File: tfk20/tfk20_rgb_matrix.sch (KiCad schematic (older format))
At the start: 40 parts

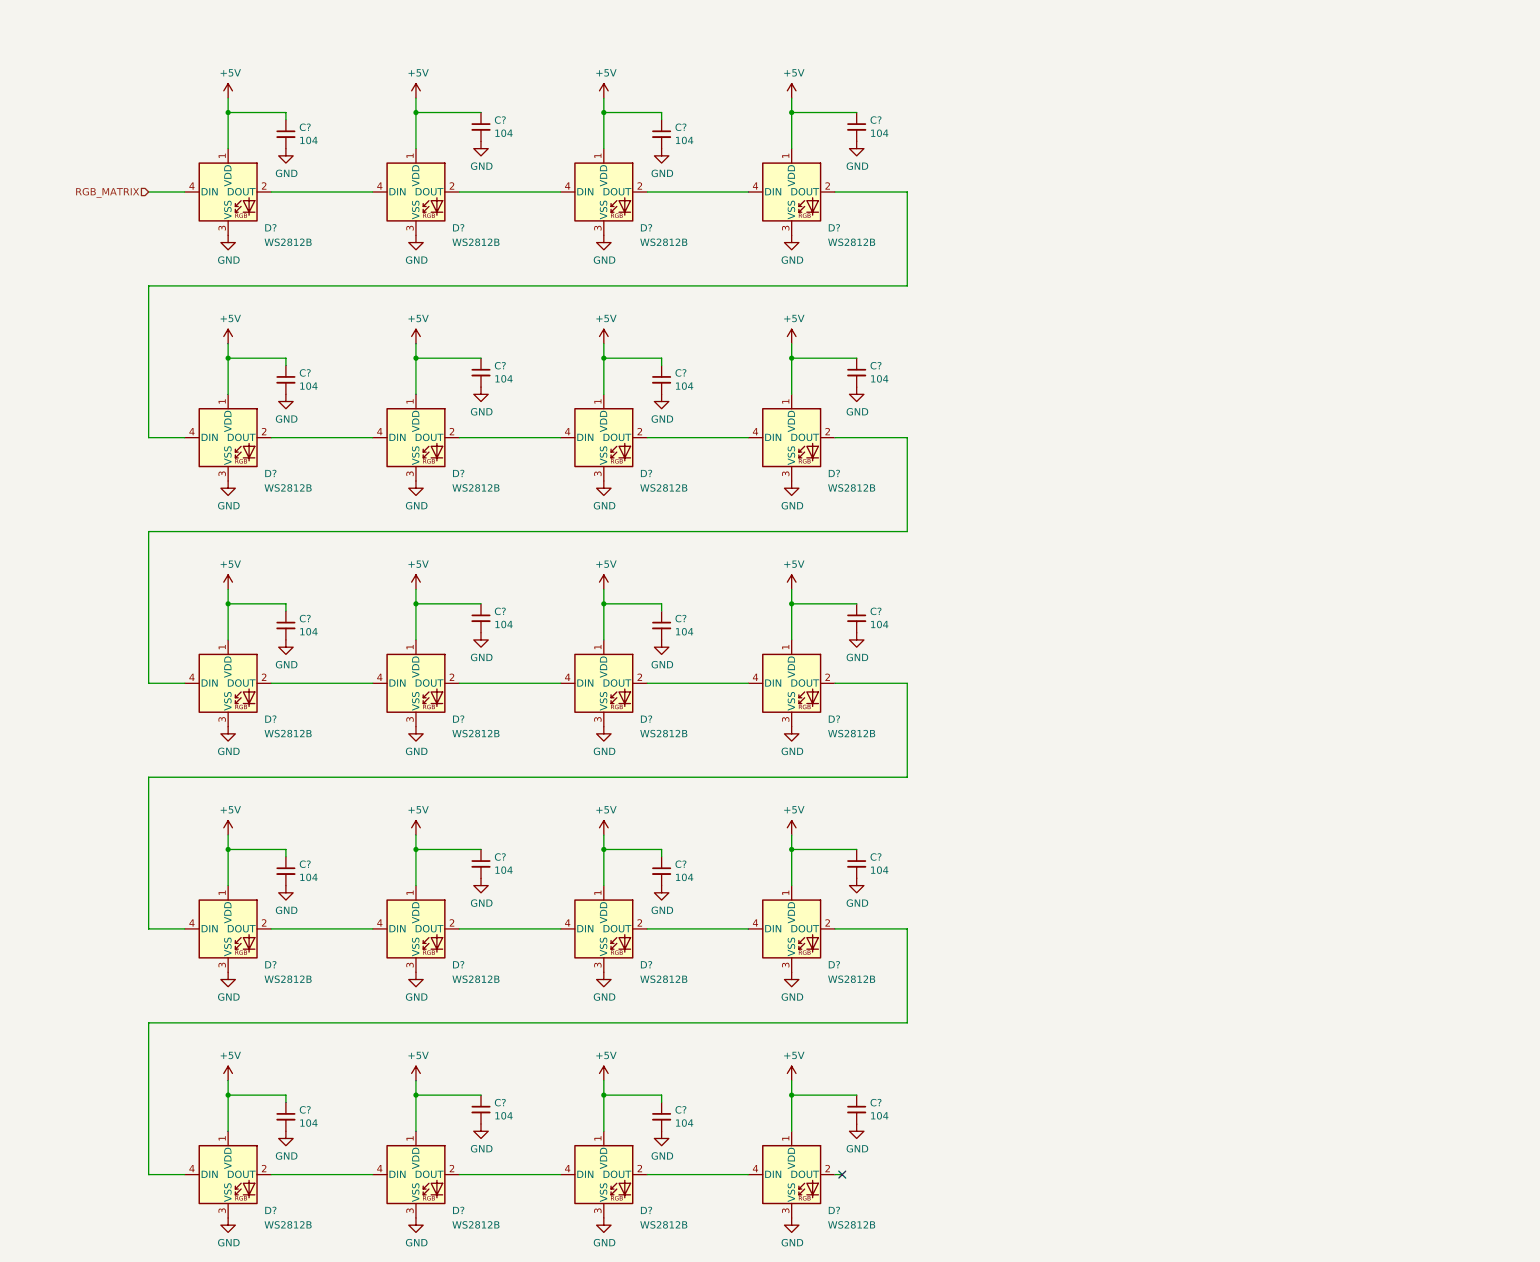
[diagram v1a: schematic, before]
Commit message: RGB LED driver
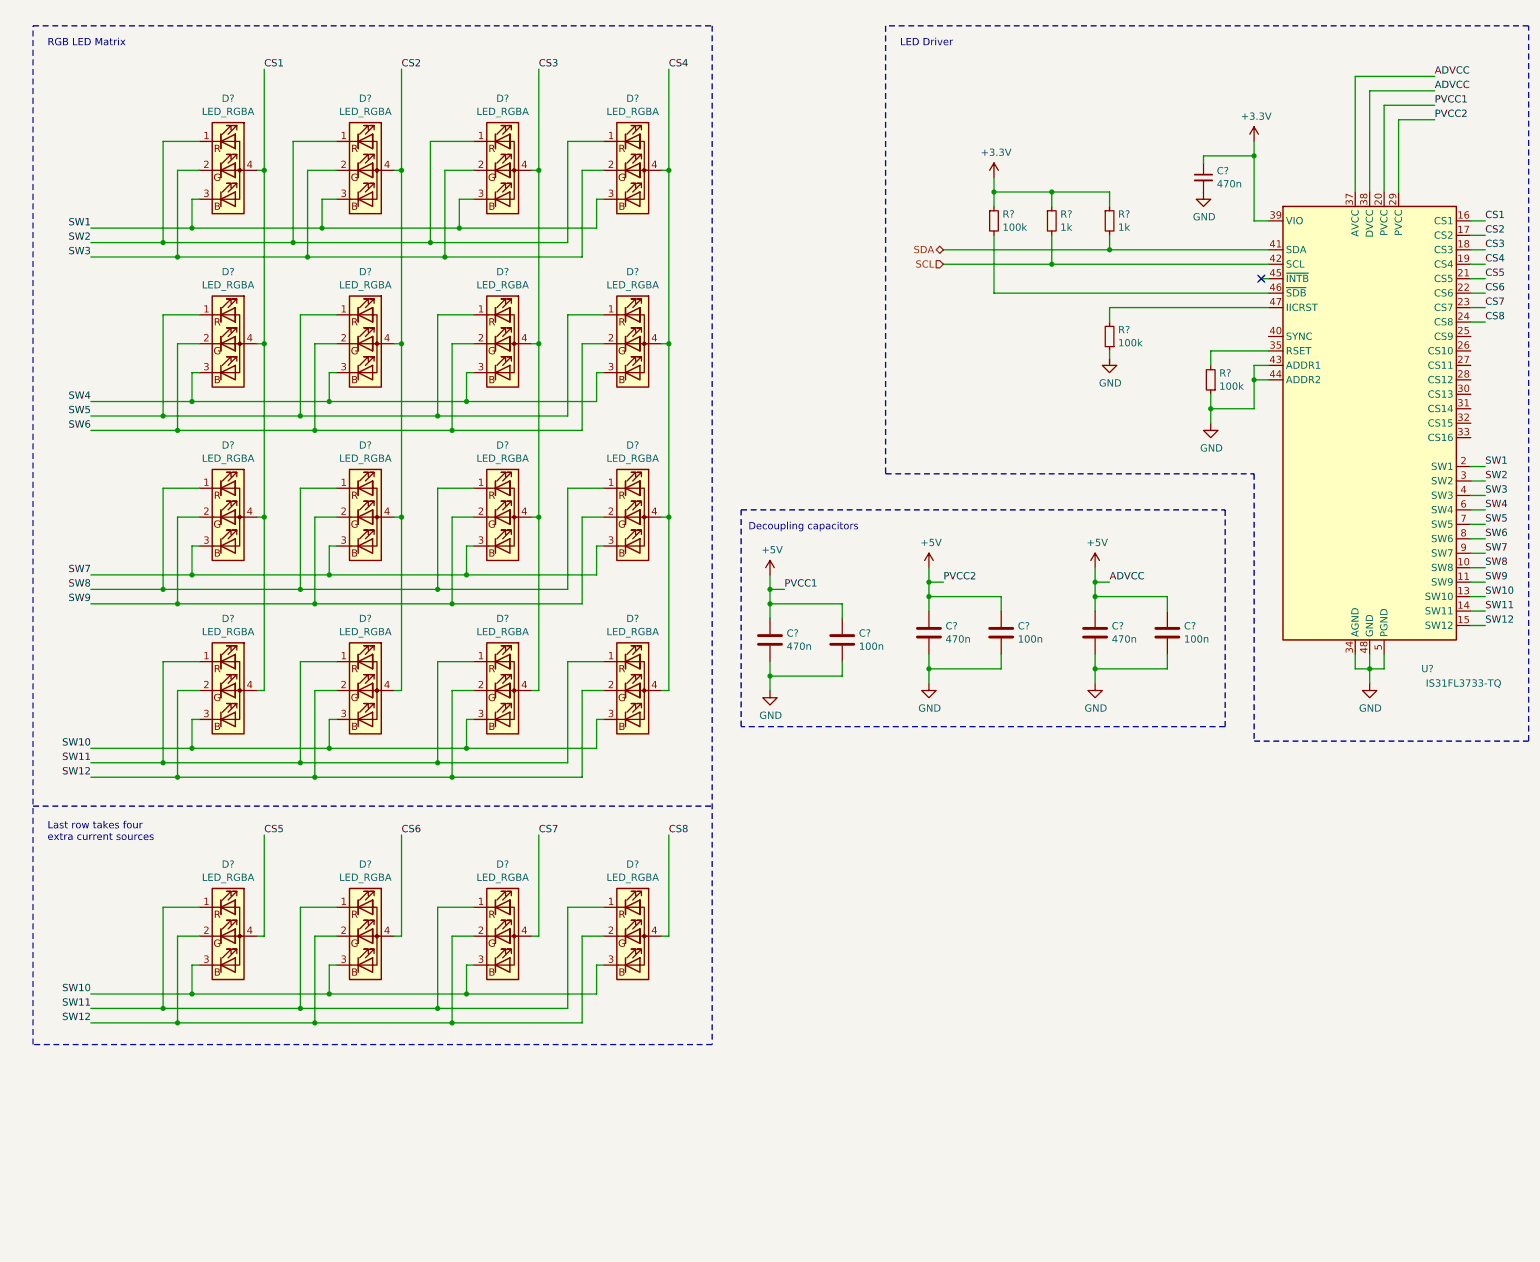
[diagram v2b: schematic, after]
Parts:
- removed C? (x20): 104, symbol Device:C_Small
- removed D? (x20): WS2812B, LED_SMD:LED_WS2812B_PLCC4_5.0x5.0mm_P3.2mm, symbol LED:WS2812B
- added C?: 470n, symbol Device:C_Small
- added C? (x3): 470n, symbol Device:C
- added C? (x3): 100n, symbol Device:C
- added D? (x20): LED_RGBA, symbol Device:LED_RGBA
- added R? (x3): 100k, symbol Device:R_Small
- added R? (x2): 1k, symbol Device:R_Small
- added U?: IS31FL3733-TQ, Package_QFP:TQFP-48-1EP_7x7mm_P0.5mm_EP5x5mm, symbol Driver_LED:IS31FL3733-TQ
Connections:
- net +5V: now also C?.1, C?.1, C?.1, C?.1, C?.1, C?.2, U?.20 (PVCC), U?.29 (PVCC), U?.37 (AVCC), U?.38 (DVCC)
- net GND: now also C?.1, C?.2, C?.2, C?.2, C?.2, C?.2, C?.2, R?.1, R?.1, U?.12 (PGND), U?.34 (AGND), U?.43 (ADDR1), U?.44 (ADDR2), U?.48 (GND), U?.49 (GND), U?.5 (PGND)
- new net: R?.2, U?.35 (RSET)
- new net: R?.2, U?.46 (~SDB)
- new net: R?.2, U?.47 (IICRST)
- new net +3V3: C?.1, R?.1, R?.1, R?.1, U?.39 (VIO)
- new net CS1: D?.4 (A), D?.4 (A), D?.4 (A), D?.4 (A), U?.16 (CS1)
- new net CS2: D?.4 (A), D?.4 (A), D?.4 (A), D?.4 (A), U?.17 (CS2)
- new net CS3: D?.4 (A), D?.4 (A), D?.4 (A), D?.4 (A), U?.18 (CS3)
- new net CS4: D?.4 (A), D?.4 (A), D?.4 (A), D?.4 (A), U?.19 (CS4)
- new net CS5: D?.4 (A), U?.21 (CS5)
- new net CS6: D?.4 (A), U?.22 (CS6)
- new net CS7: D?.4 (A), U?.23 (CS7)
- new net CS8: D?.4 (A), U?.24 (CS8)
- new net SCL: R?.2, U?.42 (SCL)
- new net SDA: R?.2, U?.41 (SDA)
- new net SW1: D?.3 (BK), D?.3 (BK), D?.3 (BK), D?.3 (BK), U?.2 (SW1)
- new net SW10: D?.3 (BK), D?.3 (BK), D?.3 (BK), D?.3 (BK), D?.3 (BK), D?.3 (BK), D?.3 (BK), D?.3 (BK), U?.13 (SW10)
- new net SW11: D?.1 (RK), D?.1 (RK), D?.1 (RK), D?.1 (RK), D?.1 (RK), D?.1 (RK), D?.1 (RK), D?.1 (RK), U?.14 (SW11)
- new net SW12: D?.2 (GK), D?.2 (GK), D?.2 (GK), D?.2 (GK), D?.2 (GK), D?.2 (GK), D?.2 (GK), D?.2 (GK), U?.15 (SW12)
- new net SW2: D?.1 (RK), D?.1 (RK), D?.1 (RK), D?.1 (RK), U?.3 (SW2)
- new net SW3: D?.2 (GK), D?.2 (GK), D?.2 (GK), D?.2 (GK), U?.4 (SW3)
- new net SW4: D?.3 (BK), D?.3 (BK), D?.3 (BK), D?.3 (BK), U?.6 (SW4)
- new net SW5: D?.1 (RK), D?.1 (RK), D?.1 (RK), D?.1 (RK), U?.7 (SW5)
- new net SW6: D?.2 (GK), D?.2 (GK), D?.2 (GK), D?.2 (GK), U?.8 (SW6)
- new net SW7: D?.3 (BK), D?.3 (BK), D?.3 (BK), D?.3 (BK), U?.9 (SW7)
- new net SW8: D?.1 (RK), D?.1 (RK), D?.1 (RK), D?.1 (RK), U?.10 (SW8)
- new net SW9: D?.2 (GK), D?.2 (GK), D?.2 (GK), D?.2 (GK), U?.11 (SW9)
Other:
- note added: "Decoupling capacitors"
- note added: "LED Driver"
- note added: "Last row takes four \nextra current sources"
- note added: "RGB LED Matrix"

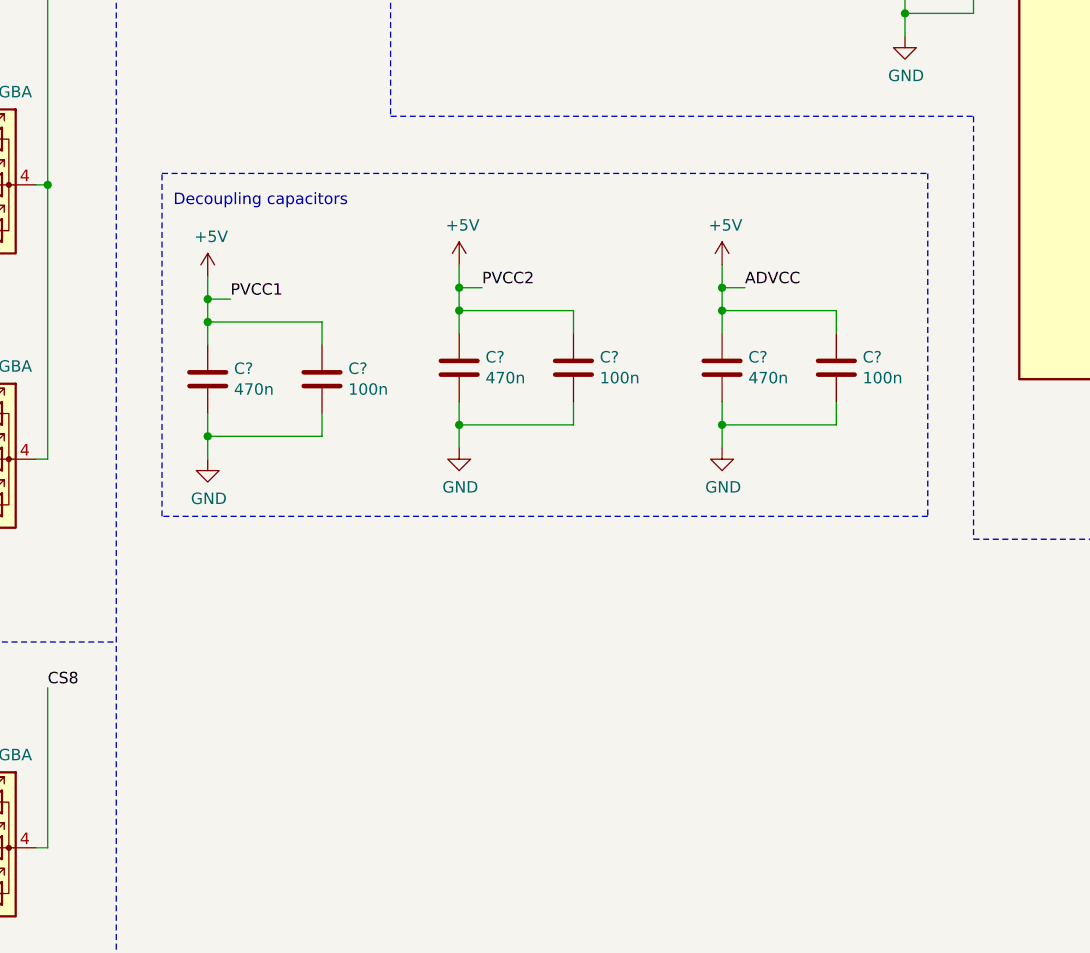
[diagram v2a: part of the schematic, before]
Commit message: Change caps layout
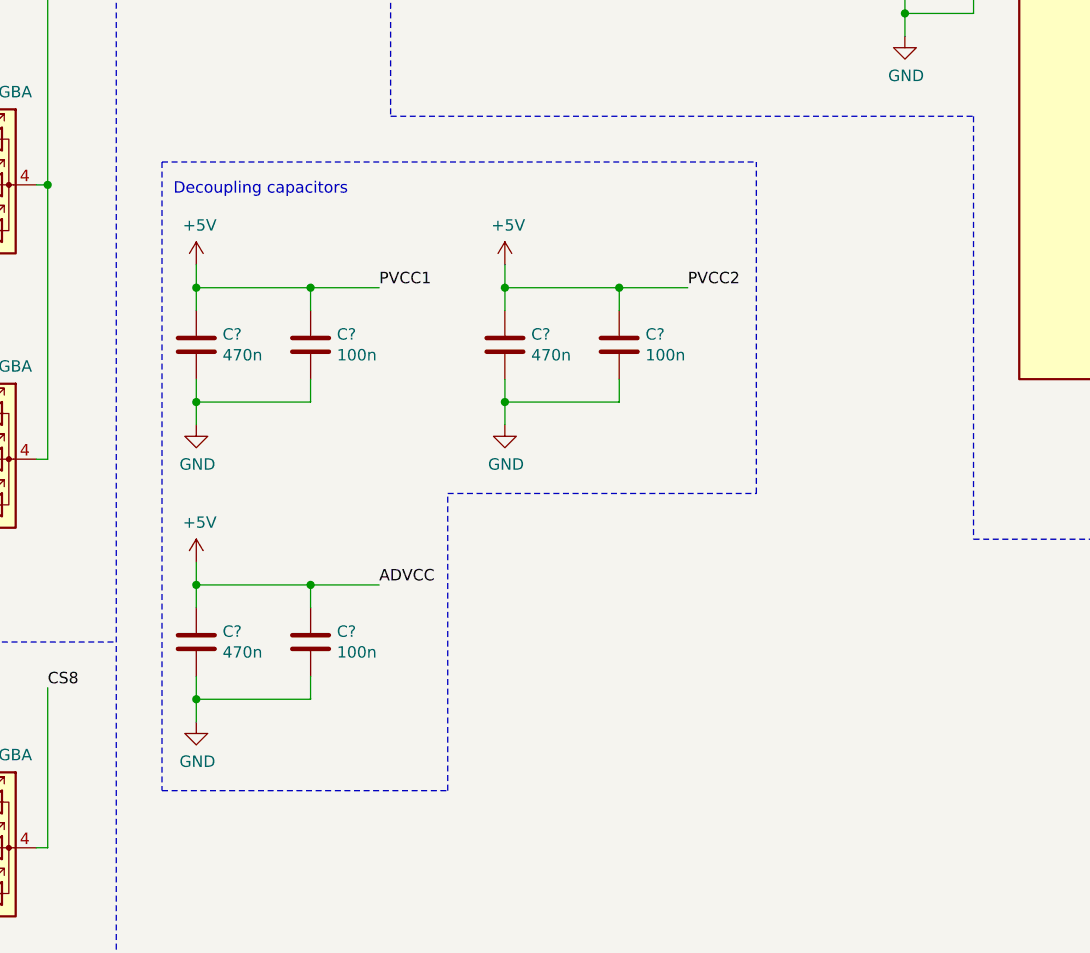
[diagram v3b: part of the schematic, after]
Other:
- moved on the sheet: C?

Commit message: Change MCU, add another row, add reset button
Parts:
- removed D? (x20): LED_RGBA, symbol Device:LED_RGBA
- added D33, D34, D35, D36, D37, D38, D39, D40, D41, D42, D43, D44, D45, D46, D47, D48, D49, D50, D51, D52, D53, D54, D55, D56: LED_RGBA, symbol Device:LED_RGBA
- gave numbers to parts that had none: 13
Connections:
- net CS1: now also D33.4 (A), D35.4 (A), D37.4 (A)
- net CS2: now also D39.4 (A), D41.4 (A), D43.4 (A)
- net CS3: now also D45.4 (A), D47.4 (A), D49.4 (A)
- net CS4: now also D51.4 (A), D53.4 (A), D55.4 (A)
- net CS5: now also D34.4 (A), D36.4 (A), D38.4 (A)
- net CS6: now also D40.4 (A), D42.4 (A), D44.4 (A)
- net CS7: now also D46.4 (A), D48.4 (A), D50.4 (A)
- net CS8: now also D52.4 (A), D54.4 (A), D56.4 (A)
- net SW1: now also D33.3 (BK), D34.3 (BK), D39.3 (BK), D40.3 (BK), D45.3 (BK), D46.3 (BK), D51.3 (BK), D52.3 (BK)
- net SW2: now also D33.1 (RK), D34.1 (RK), D39.1 (RK), D40.1 (RK), D45.1 (RK), D46.1 (RK), D51.1 (RK), D52.1 (RK)
- net SW3: now also D33.2 (GK), D34.2 (GK), D39.2 (GK), D40.2 (GK), D45.2 (GK), D46.2 (GK), D51.2 (GK), D52.2 (GK)
- net SW4: now also D35.3 (BK), D36.3 (BK), D41.3 (BK), D42.3 (BK), D47.3 (BK), D48.3 (BK), D53.3 (BK), D54.3 (BK)
- net SW5: now also D35.1 (RK), D36.1 (RK), D41.1 (RK), D42.1 (RK), D47.1 (RK), D48.1 (RK), D53.1 (RK), D54.1 (RK)
- net SW6: now also D35.2 (GK), D36.2 (GK), D41.2 (GK), D42.2 (GK), D47.2 (GK), D48.2 (GK), D53.2 (GK), D54.2 (GK)
- net SW7: now also D37.3 (BK), D38.3 (BK), D43.3 (BK), D44.3 (BK), D49.3 (BK), D50.3 (BK), D55.3 (BK), D56.3 (BK)
- net SW8: now also D37.1 (RK), D38.1 (RK), D43.1 (RK), D44.1 (RK), D49.1 (RK), D50.1 (RK), D55.1 (RK), D56.1 (RK)
- net SW9: now also D37.2 (GK), D38.2 (GK), D43.2 (GK), D44.2 (GK), D49.2 (GK), D50.2 (GK), D55.2 (GK), D56.2 (GK)
- net SW10: no longer names the net of U4.13 (SW10)
- net SW11: no longer names the net of U4.14 (SW11)
- net SW12: no longer names the net of U4.15 (SW12)
- no-connect marks 1 -> 13
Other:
- note added: "3 switches and\n8 current sources\nper 2 rows on pad"
- note added: "Decoupling capacitors for LED driver"
- note added: "I2C termination \npull-ups"
- note removed: "Decoupling capacitors"
- note removed: "Last row takes four \nextra current sources"
